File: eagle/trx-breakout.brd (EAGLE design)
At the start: 40.1 x 35.5 mm, 8 parts, among them Q1 BSS84, Q2 BSS84, Q3 BSS123, Q4 BSS123

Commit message: Added basic auto-route
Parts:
- added J1: DF12NB(3.0)-10DX-0.5VHRS_DF12NB(3.0)-10DS-0.5V, con-hirose2:HRS_DF12NB(3.0)-10DS-0.5V
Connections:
- new net N$10: J1.8
- new net N$8: J1.4
- new net N$9: J1.6
- net +5V: now also J1.1, J1.2
- net GND: now also J1.10, J1.9
- net PWR_TRIG: now also J1.3
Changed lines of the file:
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@@
 </element>
 <element name="U$1" library="texas-instruments" library_urn="urn:adsk.eagle:library:17599867" package="SOT-23-5" package3d_urn="urn:adsk.eagle:package:40577305/2" value="SN74LVC1G80" x="7.62" y="15.24" smashed="yes" rot="R90"/>
+<element name="J1" library="con-hirose2" library_urn="urn:adsk.eagle:library:40899389" package="HRS_DF12NB(3.0)-10DS-0.5V" package3d_urn="urn:adsk.eagle:package:40903384/2" value="DF12NB(3.0)-10DX-0.5VHRS_DF12NB(3.0)-10DS-0.5V" x="20.32" y="19.05" smashed="yes">
+<attribute name="NAME" x="16.92" y="22.4" size="1.27" layer="25"/>
+</element>
 </elements>
 <signals>
@@
 <contactref element="U$1" pad="5"/>
 <contactref element="Q2" pad="2"/>
+<contactref element="J1" pad="2"/>
+<contactref element="J1" pad="1"/>
 <wire x1="8.57" y1="3.98" x2="22.54" y2="3.98" width="0" layer="19" extent="1-1"/>
 <wire x1="6.67" y1="10.16" x2="8.57" y2="3.98" width="0" layer="19" extent="1-1"/>
 <wire x1="6.67" y1="16.54" x2="6.67" y2="10.16" width="0" layer="19" extent="1-1"/>
+<wire x1="19.32" y1="20.85" x2="6.67" y2="10.16" width="0" layer="19" extent="1-1"/>
+<wire x1="19.32" y1="17.25" x2="19.32" y2="20.85" width="0" layer="19" extent="1-1"/>
 </signal>
 <signal name="N$2">
@@
 <contactref element="U$1" pad="3"/>
 <contactref element="Q3" pad="2"/>
+<contactref element="J1" pad="9"/>
+<contactref element="J1" pad="10"/>
 <wire x1="14.92" y1="3.98" x2="27.62" y2="3.98" width="0" layer="19" extent="1-1"/>
 <wire x1="13.65" y1="10.16" x2="14.92" y2="3.98" width="0" layer="19" extent="1-1"/>
 <wire x1="8.57" y1="13.94" x2="13.65" y2="10.16" width="0" layer="19" extent="1-1"/>
+<wire x1="21.32" y1="20.85" x2="8.57" y2="13.94" width="0" layer="19" extent="1-1"/>
+<wire x1="21.32" y1="17.25" x2="21.32" y2="20.85" width="0" layer="19" extent="1-1"/>
 </signal>
 <signal name="N$5">
@@
 <contactref element="Q3" pad="3"/>
 <contactref element="Q2" pad="3"/>
+<contactref element="J1" pad="3"/>
 <wire x1="7.62" y1="6.18" x2="26.67" y2="6.18" width="0" layer="19" extent="1-1"/>
+<wire x1="19.82" y1="17.25" x2="7.62" y2="6.18" width="0" layer="19" extent="1-1"/>
+</signal>
+<signal name="N$8">
+<contactref element="J1" pad="4"/>
+</signal>
+<signal name="N$9">
+<contactref element="J1" pad="6"/>
+</signal>
+<signal name="N$10">
+<contactref element="J1" pad="8"/>
 </signal>
 </signals>

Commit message: Finalized alpha design
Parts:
- added C2: 2.2uF, rcl:C0805
- added C3: 4.7uF, rcl:C0805
- added U$2: PTS530, switches-ck:PTS530
- added U$3: TPS61240, texas-instruments:WSON6-2.0X2.0
- added U$4: 1uH, inductor-vishay:1212BZ
- added U$5, U$6, U$7: ARGB_LED, led:LED4020
- moved Q2 26.7 mm to (31.0, 18.0), flipped to the bottom
- moved R1 19.7 mm to (26.0, 3.00), flipped to the bottom, turned to 180 degrees
- moved Q4 14.4 mm to (26.0, 13.0), flipped to the bottom
- moved U$1 14.3 mm to (20.0, 8.00), flipped to the bottom, turned to 270 degrees
- moved Q1 13.7 mm to (26.0, 18.0), flipped to the bottom
- moved C1 10.2 mm to (20.0, 3.00), flipped to the bottom
- moved Q3 9.03 mm to (31.0, 13.0), flipped to the bottom
- moved R2 8.50 mm to (26.0, 8.00), flipped to the bottom
- moved J1 3.56 mm to (20.0, 15.5), flipped to the bottom
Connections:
- removed net N$10: J1.8
- removed net N$8: J1.4
- removed net N$9: J1.6
- new net +3V3: C2.1, J1.2, U$3.4, U$3.6, U$4.1
- new net LED_D: J1.4, U$5.1, U$6.1, U$7.1
- new net N$6: Q1.1, Q4.1, R1.2, U$2.3, U$2.4
- new net VBAT: J1.1, Q1.2, R1.1
- net +5V: now also C3.1, U$3.2, U$3.3, U$5.2, U$6.2, U$7.2; no longer J1.1, J1.2, Q1.2, R1.1
- net GND: now also C2.2, C3.2, U$2.1, U$2.2, U$3.1, U$5.4, U$6.4
- net N$1: now also U$3.5, U$4.2; no longer Q1.1, Q4.1, R1.2
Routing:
- net LED_D: track 0.00 -> 66.1 mm, vias 0 -> 1
- net +5V: track 0.00 -> 59.9 mm, vias 0 -> 2
- net N$6: track 0.00 -> 41.7 mm, vias 0 -> 2
- net N$5: track 0.00 -> 39.5 mm
- net +3V3: track 0.00 -> 33.9 mm
- net VBAT: track 0.00 -> 30.2 mm
- net GND: track 0.00 -> 29.3 mm, vias 0 -> 1
- net PWR_TRIG: track 0.00 -> 21.4 mm, vias 0 -> 2
- net N$3: track 0.00 -> 19.8 mm
- net N$2: track 0.00 -> 13.3 mm, vias 0 -> 2
- net N$1: track 0.00 -> 9.77 mm
- added copper zone on layer 1, net GND
- added copper zone on layer 16, net GND
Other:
- outline, holes or cut-outs redrawn

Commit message: Added new layout and gerber files
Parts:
- C1: value (none) -> 2.2uF
- C2: value 2.2uF -> 4.7uF
- R1: value (none) -> 100k
- R2: value (none) -> 200k
- moved C1 10.8 mm to (14.0, 12.0), turned to 180 degrees
- moved C2 9.00 mm to (14.0, 3.00)
- moved C3 6.00 mm to (20.0, 3.00)
- moved Q3 5.00 mm to (26.0, 13.0)
- moved Q4 5.00 mm to (31.0, 13.0)
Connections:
- new net N$4: Q1.1, Q3.1, R1.2, U$2.3, U$2.4
- new net N$7: Q2.2
- net +3V3: now also C1.1; no longer C2.1
- net +5V: now also C2.1; no longer C3.1, Q2.2, U$1.5
- net GND: now also U$7.4
- net N$3: now also C3.1, Q3.3; no longer C1.1, Q4.3
- net N$5: now also Q4.1; no longer Q3.1
- net N$6: now also U$1.5; no longer Q1.1, Q4.1, R1.2, U$2.3, U$2.4
- net PWR_TRIG: now also Q4.3; no longer Q3.3
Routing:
- net GND: track 29.3 -> 91.7 mm, vias 1 -> 4
- net N$6: track 41.7 -> 0.00 mm, vias 2 -> 0
- net N$4: track 0.00 -> 24.1 mm, vias 0 -> 1
- net +5V: track 59.9 -> 50.6 mm
- net N$5: track 39.5 -> 32.9 mm
- net LED_D: track 66.1 -> 60.7 mm
- net VBAT: track 30.2 -> 26.5 mm, vias 0 -> 2
- net N$3: track 19.8 -> 18.0 mm
- net PWR_TRIG: track 21.4 -> 20.5 mm, vias 2 -> 0
- net +3V3: track 33.9 -> 34.8 mm
- net N$2: track 13.3 -> 12.6 mm

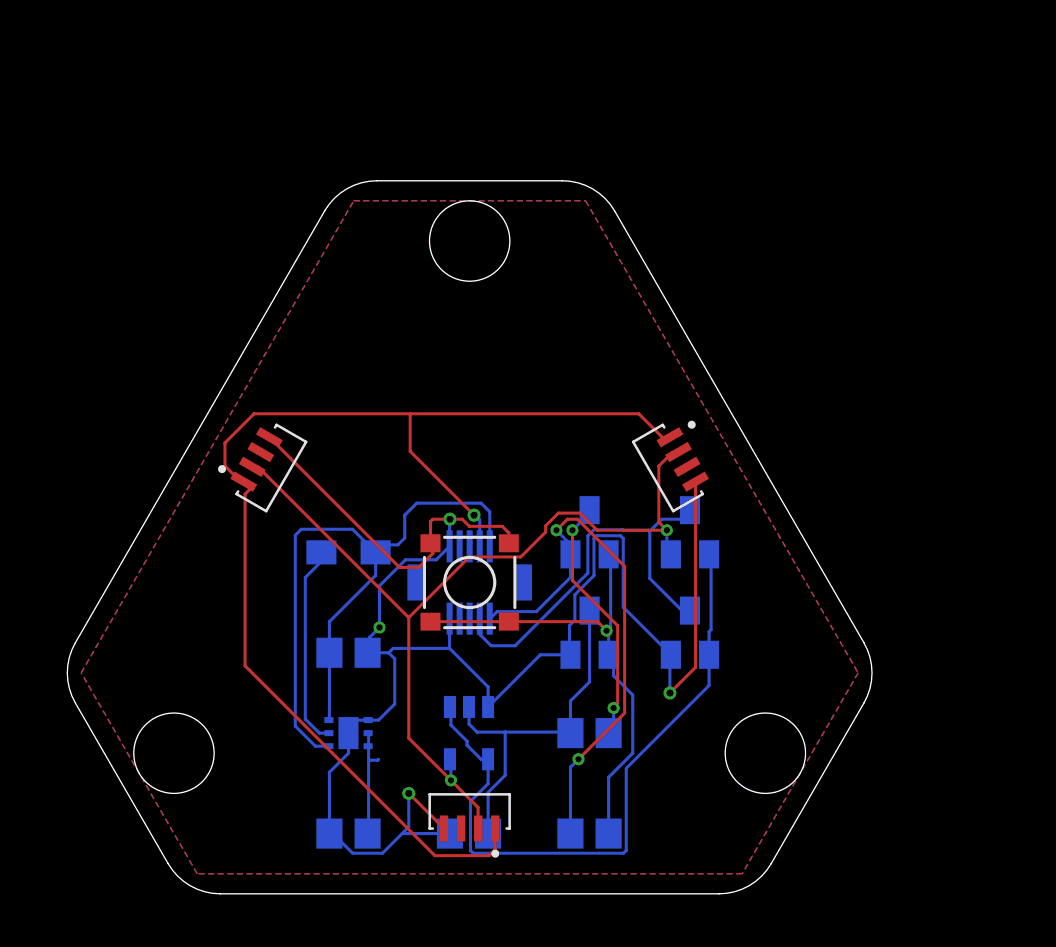
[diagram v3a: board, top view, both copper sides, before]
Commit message: Designed new boards wit fixed errors
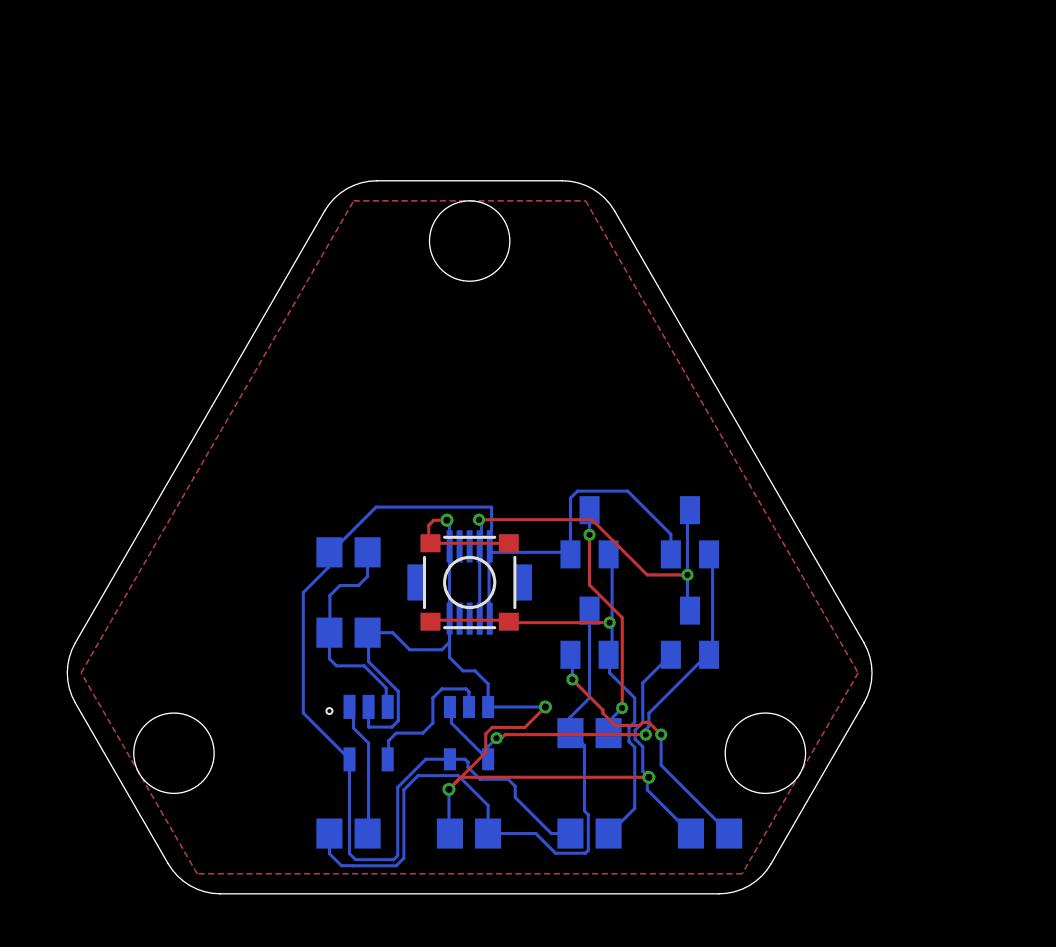
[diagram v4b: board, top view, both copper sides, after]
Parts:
- removed C1: 2.2uF, rcl:C0805
- removed C2: 4.7uF, rcl:C0805
- removed U$3: TPS61240, texas-instruments:WSON6-2.0X2.0
- removed U$4: 1uH, inductor-vishay:1212BZ
- removed U$5, U$6, U$7: ARGB_LED, led:LED4020
- added IC1: LMV321M5X, linear:SOT23-5
- added R3, R5: 200k, rcl:R0805
- added R4, R6: 10k, rcl:R0805
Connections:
- removed net +3V3: C1.1, J1.2, U$3.4, U$3.6, U$4.1
- removed net +5V: C2.1, U$3.2, U$3.3, U$5.2, U$6.2, U$7.2
- removed net LED_D: J1.4, U$5.1, U$6.1, U$7.1
- new net N$8: Q3.2, R6.1
- net GND: now also IC1.2, R3.1, R6.2; no longer C1.2, C2.2, Q3.2, U$3.1, U$5.4, U$6.4, U$7.4
- net N$1: now also IC1.3, R3.2, R5.1; no longer U$3.5, U$4.2
- net N$3: now also R4.2; no longer U$1.2
- net N$6: now also IC1.1, R4.1; no longer U$1.5
- net N$7: now also IC1.4, U$1.2; no longer Q2.2
- net PWR_TRIG: now also J1.4
- net VBAT: now also IC1.5, J1.2, Q2.2, R5.2, U$1.5
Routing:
- net LED_D: track 60.7 -> 0.00 mm, vias 1 -> 0
- net +5V: track 50.6 -> 0.00 mm, vias 2 -> 0
- net VBAT: track 26.5 -> 63.2 mm, vias 2 -> 0
- net +3V3: track 34.8 -> 0.00 mm
- net GND: track 91.7 -> 61.8 mm
- net N$3: track 18.0 -> 33.4 mm
- net N$8: track 0.00 -> 13.4 mm, vias 0 -> 2
- net N$5: track 32.9 -> 22.5 mm, vias 0 -> 2
- net N$7: track 0.00 -> 7.64 mm
- net N$6: track 0.00 -> 6.76 mm
- net PWR_TRIG: track 20.5 -> 22.7 mm, vias 0 -> 2
- net N$1: track 10.1 -> 11.1 mm

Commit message: Reworked breakout board
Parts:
- removed IC1: LMV321M5X, linear:SOT23-5
- removed R3, R5: 200k, rcl:R0805
- removed R4, R6: 10k, rcl:R0805
- U$1: value SN74LVC1G80 -> SN74HCS72/4; device texas-instruments:SOT-23-5 -> texas-instruments:TSSOP14
- moved U$1 10.6 mm to (12.0, 15.0), turned to 90 degrees
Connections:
- removed net N$6: IC1.1, R4.1
- removed net N$7: IC1.4, U$1.2
- removed net N$8: Q3.2, R6.1
- net GND: now also Q3.2, U$1.10, U$1.11, U$1.12, U$1.13, U$1.7; no longer IC1.2, R3.1, R6.2, U$1.3
- net N$1: now also Q1.3, Q3.3, R2.1; no longer IC1.3, R3.2, R5.1
- net N$2: now also U$1.2, U$1.6; no longer Q1.3, R2.1
- net N$3: now also U$1.3; no longer Q3.3, R4.2
- net N$5: no longer U$1.1, U$1.4
- net VBAT: now also U$1.1, U$1.14, U$1.4; no longer IC1.5, R5.2, U$1.5
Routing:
- net VBAT: track 63.2 -> 0.00 mm
- net GND: track 61.8 -> 0.00 mm, vias 4 -> 0
- net N$3: track 33.4 -> 0.00 mm
- net N$4: track 24.5 -> 0.00 mm, vias 1 -> 0
- net PWR_TRIG: track 22.7 -> 0.00 mm, vias 2 -> 0
- net N$5: track 22.5 -> 0.00 mm, vias 2 -> 0
- net N$8: track 13.4 -> 0.00 mm, vias 2 -> 0
- net N$2: track 12.1 -> 0.00 mm, vias 2 -> 0
- net N$1: track 11.1 -> 0.00 mm
- net N$7: track 7.64 -> 0.00 mm
- net N$6: track 6.76 -> 0.00 mm

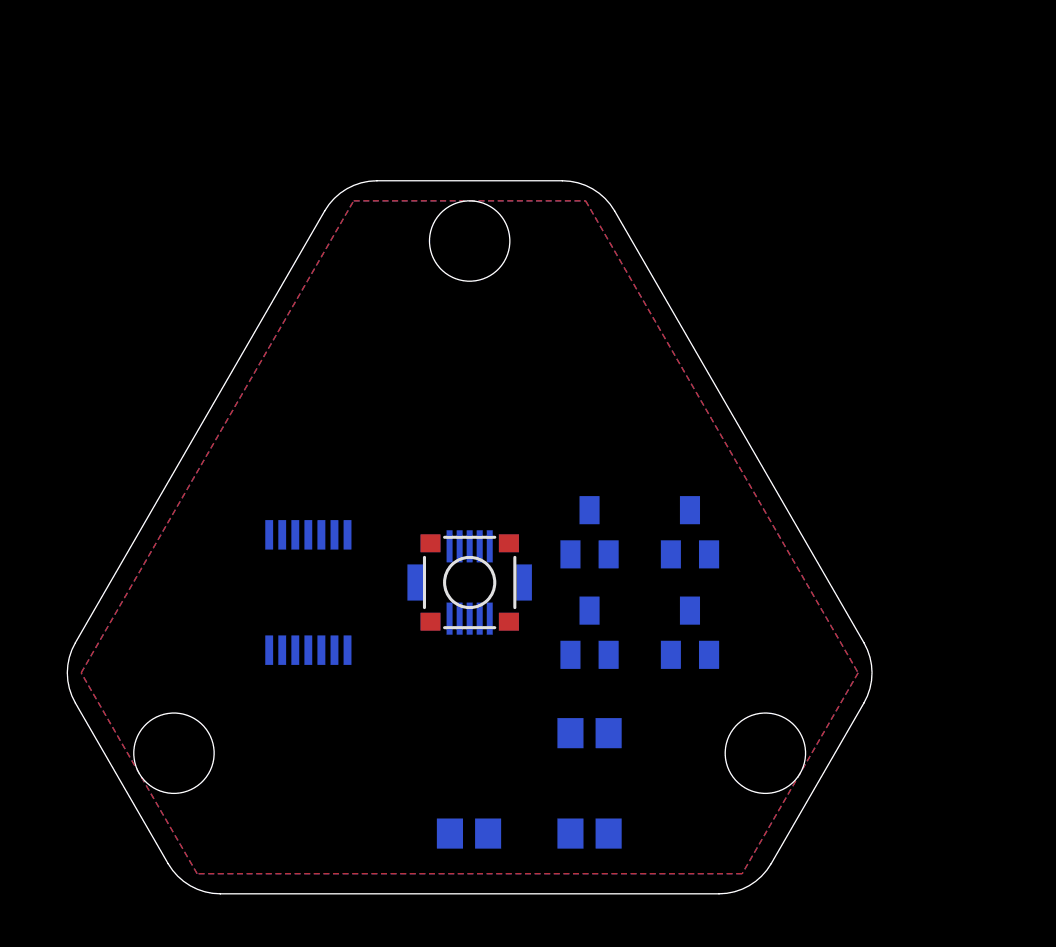
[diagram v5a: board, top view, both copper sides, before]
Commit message: Modified board layout
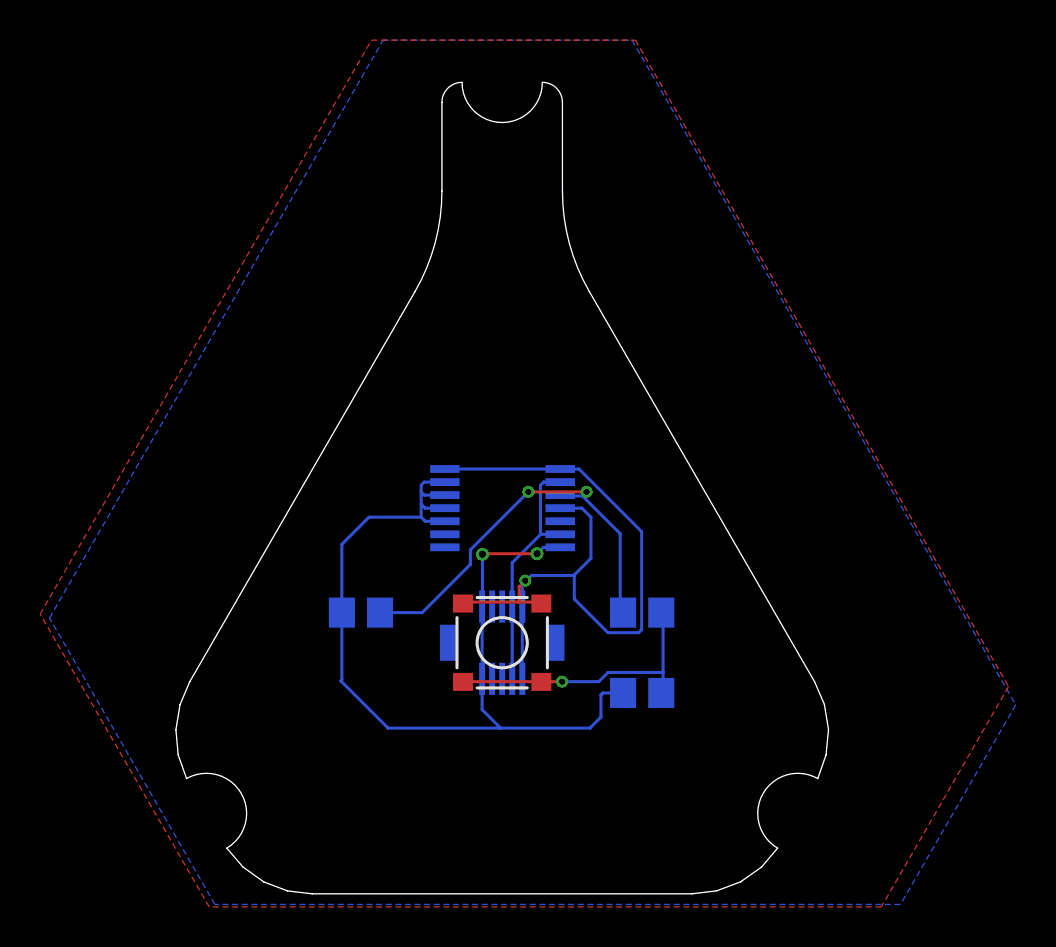
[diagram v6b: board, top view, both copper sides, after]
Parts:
- removed Q1, Q2: BSS84, transistor-small-signal:SOT23
- removed Q3, Q4: BSS123, transistor-small-signal:SOT23
- moved C3 12.2 mm to (14.6, 14.0)
- moved U$1 10.5 mm to (21.7, 19.2), turned to 0 degrees
- moved R1 7.47 mm to (28.6, 10.0)
- moved R2 6.55 mm to (28.6, 14.0)
- moved J1 3.41 mm to (21.7, 12.5)
- moved U$2 3.41 mm to (21.7, 12.5)
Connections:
- removed net N$1: Q1.3, Q3.3, R2.1
- removed net N$2: U$1.2, U$1.6
- removed net N$5: Q2.1, Q4.1
- net GND: now also R1.1; no longer Q3.2, Q4.2, U$2.1, U$2.2
- net N$4: now also R2.1; no longer Q1.1, Q3.1
- net PWR_TRIG: now also U$1.2, U$1.6; no longer Q2.3, Q4.3
- net VBAT: now also U$2.1, U$2.2; no longer Q1.2, Q2.2, R1.1
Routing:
- net GND: track 0.00 -> 47.4 mm, vias 0 -> 2
- net VBAT: track 0.00 -> 39.0 mm, vias 0 -> 1
- net N$3: track 0.00 -> 21.3 mm, vias 0 -> 2
- net N$4: track 0.00 -> 14.2 mm, vias 0 -> 1
- net PWR_TRIG: track 0.00 -> 12.3 mm
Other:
- board size 40.1 x 35.5 mm -> 32.5 x 40.4 mm
